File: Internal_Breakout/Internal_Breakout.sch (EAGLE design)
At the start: 21 parts, among them Q1 FDN360P, U1 LP2985AIM5-3.3

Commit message: Slight changes to Internal Breakout
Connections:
- net GND: now also U1.GND
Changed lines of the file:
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@@
 <pinref part="C1" gate="G$1" pin="2"/>
 <wire x1="104.14" y1="139.7" x2="104.14" y2="127" width="0.1524" layer="91"/>
-<wire x1="104.14" y1="127" x2="132.08" y2="127" width="0.1524" layer="91"/>
+<wire x1="104.14" y1="127" x2="119.38" y2="127" width="0.1524" layer="91"/>
 <junction x="132.08" y="127"/>
 <pinref part="Q1" gate="G$1" pin="G"/>
+<wire x1="119.38" y1="127" x2="132.08" y2="127" width="0.1524" layer="91"/>
 <wire x1="93.98" y1="144.78" x2="93.98" y2="127" width="0.1524" layer="91"/>
 <wire x1="93.98" y1="127" x2="104.14" y2="127" width="0.1524" layer="91"/>
 <junction x="104.14" y="127"/>
 <pinref part="C6" gate="G$1" pin="2"/>
+<pinref part="U1" gate="G$1" pin="GND"/>
+<wire x1="119.38" y1="139.7" x2="119.38" y2="127" width="0.1524" layer="91"/>
+<junction x="119.38" y="127"/>
 </segment>
 <segment>

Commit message: Slight Changes to Internal Breakout
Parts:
- Q1: value FDN360P -> DMP3099L
- U1: value LP2985AIM5-3.3 -> LP2985
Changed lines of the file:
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@@
 <parts>
 <part name="FRAME2" library="frames" library_urn="urn:adsk.eagle:library:229" deviceset="DINA4_L" device=""/>
-<part name="Q1" library="transistor-power" library_urn="urn:adsk.eagle:library:400" deviceset="FDN360P" device="" package3d_urn="urn:adsk.eagle:package:29529/2"/>
-<part name="U1" library="LP2985" deviceset="LP2985" device="AIM5-3.3"/>
+<part name="Q1" library="transistor-power" library_urn="urn:adsk.eagle:library:400" deviceset="FDN360P" device="" package3d_urn="urn:adsk.eagle:package:29529/2" value="DMP3099L"/>
+<part name="U1" library="LP2985" deviceset="LP2985" device="AIM5-3.3" value="LP2985"/>
 <part name="C1" library="rcl" library_urn="urn:adsk.eagle:library:334" deviceset="C-EU" device="C0603" package3d_urn="urn:adsk.eagle:package:23616/2" value="1uF"/>
 <part name="C2" library="rcl" library_urn="urn:adsk.eagle:library:334" deviceset="C-EU" device="C0603" package3d_urn="urn:adsk.eagle:package:23616/2" value="10uF"/>

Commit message: Fixed labels on internal breakout
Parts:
- renumbered SV1 to J1, SV10 to J12, SV11 to J8, SV12 to J7, SV13 to J9, SV2 to J2, SV3 to J13, SV4 to J6, SV5 to J3, SV6 to J4, SV7 to J10, SV8 to J11, SV9 to J5
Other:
- note added: "10/25/2018 4:41:25 PM"
- note removed: "12/29/2015 2:35:25 PM"

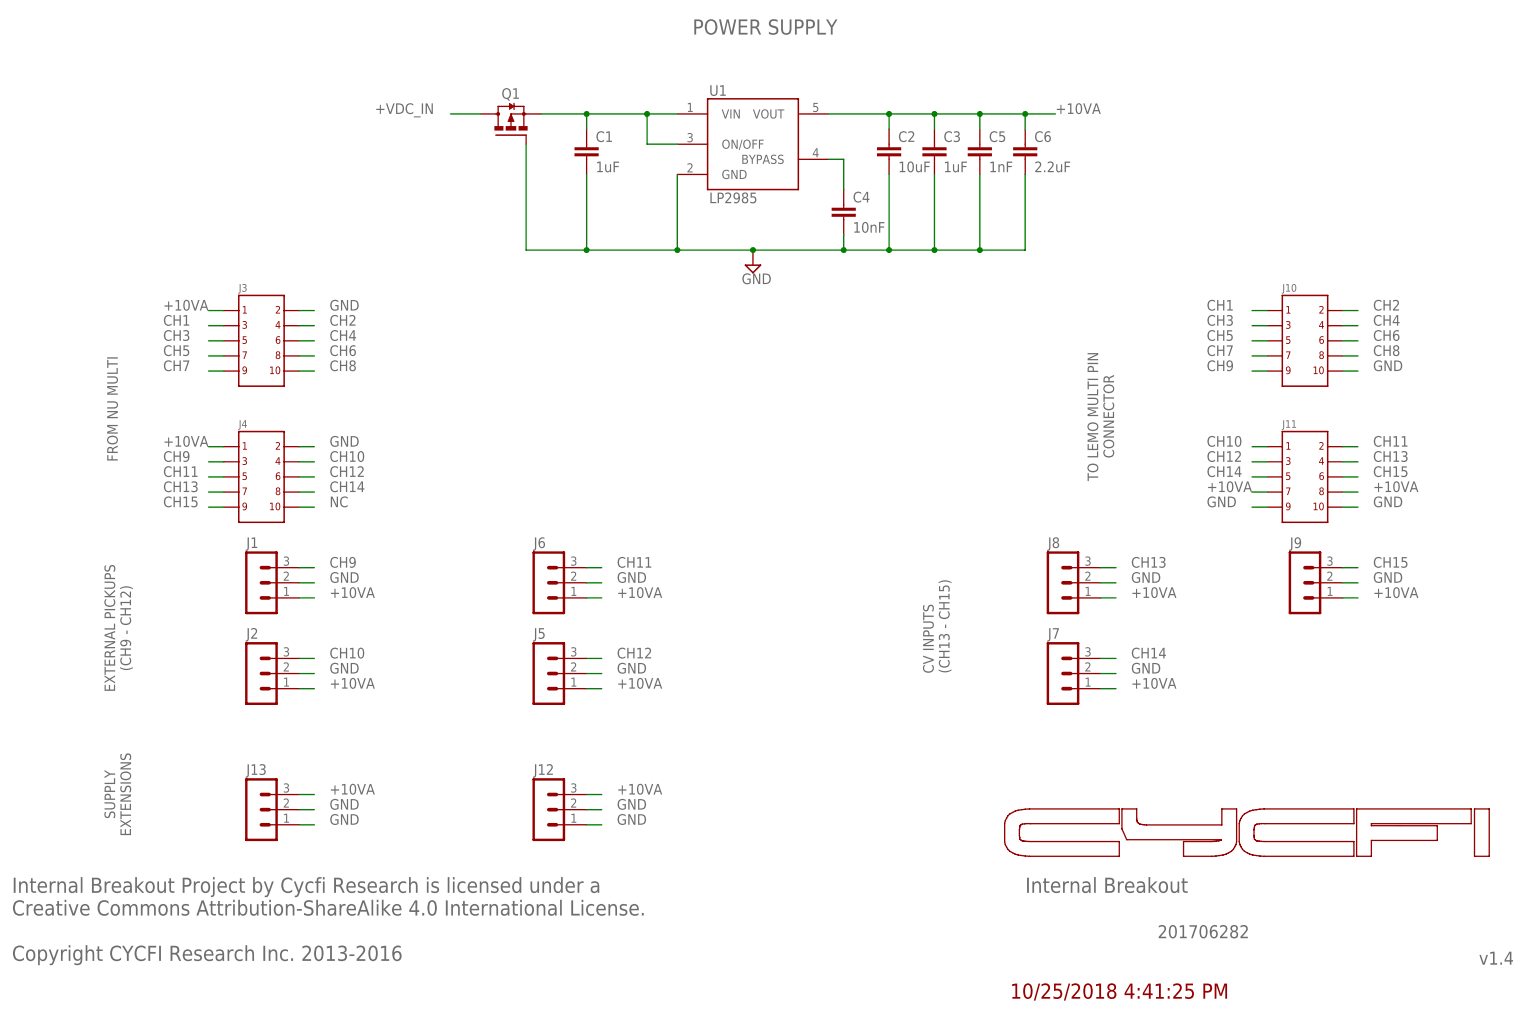
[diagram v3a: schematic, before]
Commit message: fix schematic issue, connector's triangle marking must to pin 1 of the header in the schematic
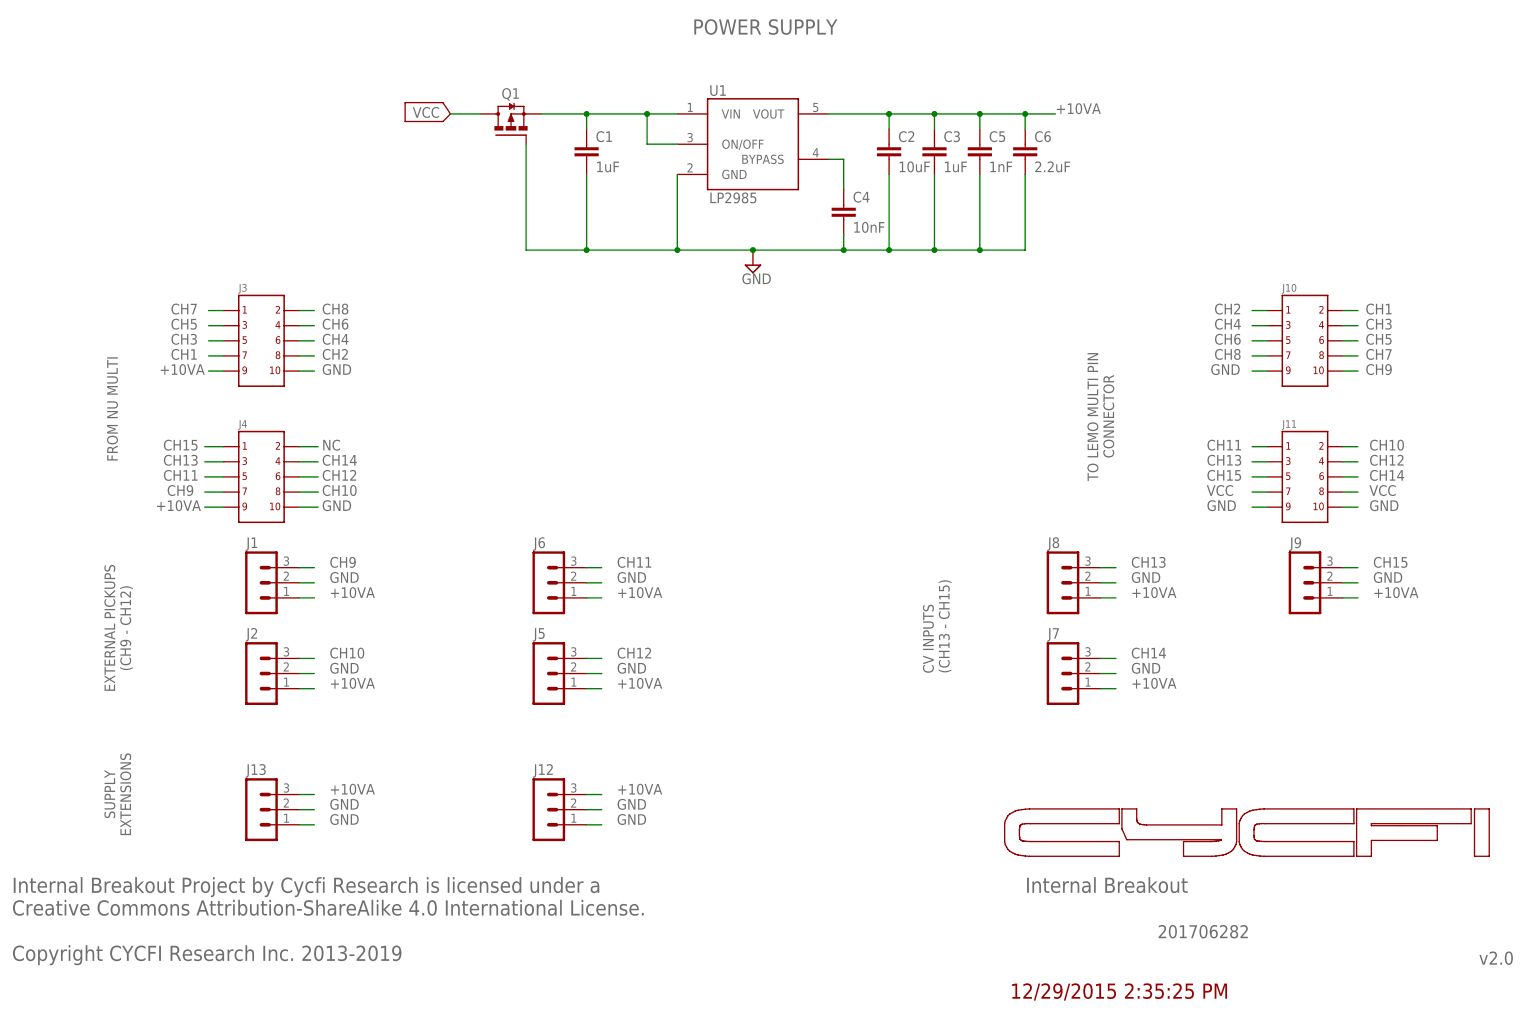
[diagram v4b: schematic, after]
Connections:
- net +VDC_IN renamed VCC
- removed net N$2: J4.10
- new net NC: J4.2
- net CH1: now also J10.2, J3.7; no longer J10.1, J3.3
- net CH10: now also J11.2, J4.8; no longer J11.1, J4.4
- net CH11: now also J11.1; no longer J11.2
- net CH12: now also J11.4; no longer J11.3
- net CH13: now also J11.3, J4.3; no longer J11.4, J4.7
- net CH14: now also J11.6, J4.4; no longer J11.5, J4.8
- net CH15: now also J11.5, J4.1; no longer J11.6, J4.9
- net CH2: now also J10.1, J3.8; no longer J10.2, J3.4
- net CH3: now also J10.4; no longer J10.3
- net CH4: now also J10.3; no longer J10.4
- net CH5: now also J10.6, J3.3; no longer J10.5, J3.7
- net CH6: now also J10.5, J3.4; no longer J10.6, J3.8
- net CH7: now also J10.8, J3.1; no longer J10.7, J3.9
- net CH8: now also J10.7, J3.2; no longer J10.8, J3.10
- net CH9: now also J10.10, J4.7; no longer J10.9, J4.3
- net GND: now also J10.9, J3.10, J4.10; no longer J10.10, J3.2, J4.2
- net V+: now also J3.9, J4.9; no longer J3.1, J4.1
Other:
- note added: "12/29/2015 2:35:25 PM"
- note added: "CH10"
- note added: "CH11"
- note added: "CH12"
- note added: "CH13"
- note added: "CH14"
- note added: "CH15"
- note added: "CH9"
- note added: "Internal Breakout Project by Cycfi Research is licensed under a Creative Commons Attribution-ShareAlike 4.0 International License. Copyright CYCFI Research Inc. 2013-2019"
- note added: "v2.0"
- note removed: "10/25/2018 4:41:25 PM"
- note removed: "Internal Breakout Project by Cycfi Research is licensed under a Creative Commons Attribution-ShareAlike 4.0 International License. Copyright CYCFI Research Inc. 2013-2016"
- note removed: "v1.4"

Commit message: push internal breakout v2.2 schematics
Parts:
- removed C4: 10nF, rcl:C-EUC0402
- removed C5: 1nF, rcl:C-EUC0402
- removed C6: 2.2uF, rcl:C-EUC0603
- added C10, C11, C7: 10uF, resistor:C-EUC0603
- added C12: 1uF, resistor:C-EUC0603
- added C13: 0.1uF, resistor:C-EUC0402
- added C8: 470pF, resistor:C-EUC0402
- added C9: 2.2uF, resistor:C-EUC0603
- added D1, D2: (no value), m-pad-2.1:D_SCHOTTKYL
- added J14, J15, J16, J17, J19: 1X3, headers(2mm):1X3
- added J18: (no value), con-lstb:MA03-1
- added JP1: (no value), pinhead-2:PINHD-2X02_2.00
- added R1, R8: 1K, resistor:R-EU_R0402
- added R10, R9: 1M, resistor:R-EU_R0402
- added R2: 18K, resistor:R-EU_R0402
- added R3, R7: 100R, resistor:R-EU_R0402
- added R4, R5: 100K, resistor:R-EU_R0402
- added R6: 10K, resistor:R-EU_R0402
- added U2: MIC5205-5V, v-reg-micrel:MIC5219BM5
- added U3: TLV2170DGKT, CYCFI_semicon:TLV2170DGKT
- C1: value 1uF -> 10uF; device rcl:C-EUC0603 -> resistor:C-EUC0603
- C2: value 10uF -> 0.01uF; device rcl:C-EUC0603 -> resistor:C-EUC0402
- C3: value 1uF -> 0.47uF; device rcl:C-EUC0603 -> resistor:C-EUC0603
- J12, J13: value (none) -> 1X3; device con-lstb:MA03-1 -> headers(2mm):1X3
- U1: value LP2985 -> TLV2170DGKT; device LP2985:LP2985AIM5-3.3 -> CYCFI_semicon:TLV2170DGKT
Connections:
- removed net BYPASS: C4.1, U1.BYPASS
- removed net CH15: J11.5, J4.1, J9.3
- removed net NC: J4.2
- new net -7V: JP1.1
- new net 5V: C11.1, C12.1, C13.1, C9.1, J1.1, J2.1, J5.1, J6.1, J7.1, J8.1, J9.1, U2.OUT
- new net CH10/SW2_IN: J14.2, J2.3
- new net CH10/SW2_OUT: J11.2, J14.1, J15.3
- new net CH15/GK_VOL_IN: J9.3, R2.1
- new net CH15/GK_VOL_OUT: J11.5, J16.3
- new net CH7/MONO_OUT: J10.8, J19.2
- new net CH8/GK_VOL_OUT: J10.7, J17.2
- new net CH9/SW1_IN: J1.3, J12.2
- new net CH9/SW1_OUT: J10.10, J12.1, J13.3
- new net N$11: R3.1, U1G$2.IN-, U1G$2.OUT
- new net N$12: C2.1, R2.2, R4.2, R5.1, U1G$2.IN+
- new net N$14: C3.2, R6.2
- new net N$15: C3.1, R10.1, R9.1, U3G$1.IN+
- new net N$16: R7.2, U3G$1.IN-, U3G$1.OUT
- new net N$17: J16.2, R3.2
- new net N$18: D1.A, J13.2
- new net N$2: J12.3, R8.1
- new net N$22: J18.3, R6.1
- new net N$26: C10.1, D1.C, R8.2
- new net N$3: C8.1, U2.ADJ
- new net N$4: C1.1, D2.C, R1.2
- new net N$5: D2.A, J15.2
- new net N$6: J14.3, R1.1
- new net N$7: J19.1, R7.1
- new net N$8: J16.1, J17.3
- new net SW1: J13.1, JP1.4
- new net SW2: J15.1, JP1.2
- net CH10: now also J4.6; no longer J11.2, J2.3, J4.8
- net CH11: now also J4.3; no longer J4.5
- net CH12: now also J4.4; no longer J4.6
- net CH13: now also J4.1; no longer J4.3
- net CH14: now also J4.2; no longer J4.4
- net CH7: now also J19.3, J4.7; no longer J10.8
- net CH8: now also J17.1, J4.8; no longer J10.7
- net CH9: now also J4.5; no longer J1.3, J10.10, J4.7
- net GND: now also C10.2, C11.2, C12.2, C13.2, C7.2, C8.2, C9.2, J18.2, R4.1, R9.2, U2.GND; no longer C3.2, C4.2, C5.2, C6.2, J12.1, J12.2, J13.1, J13.2, U1.GND
- net N$1: now also C7.1, U2.EN, U2.IN; no longer C1.1, U1.ON/OFF, U1.VIN
- net V+: no longer C2.1, C3.1, C5.1, C6.1, J1.1, J12.3, J13.3, J2.1, J5.1, J6.1, J7.1, J8.1, J9.1, U1.VOUT
- net VCC: now also J18.1, JP1.3, R10.2, R5.2
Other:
- note added: "+7V"
- note added: "AUDIO/CV INPUTS"
- note added: "GK_MONO_IN"
- note added: "GK_Vol"
- note added: "MIC5202"
- note added: "MONO"
- note added: "TO 13P OUTPUT JACK"
- note removed: "12/29/2015 2:35:25 PM"
- note removed: "201706282"
- note removed: "CH10"
- note removed: "CH11"
- note removed: "CH12"
- note removed: "CH13"
- note removed: "CH14"
- note removed: "CH15"
- note removed: "CH9"
- note removed: "CV INPUTS (CH13 - CH15)"
- note removed: "EXTERNAL PICKUPS (CH9 - CH12)"
- note removed: "Internal Breakout"
- note removed: "NC"
- note removed: "POWER SUPPLY"
- note removed: "SUPPLY EXTENSIONS"
- note removed: "v2.0"
- moved on the sheet: C1, C2, C3, J1, J10, J11, J12, J13, J2, J3, J4, J5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
